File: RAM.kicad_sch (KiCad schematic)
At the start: 45 parts, among them U1 H3, U3 K4B4G1646E-BYMA 4GB, U4 K4B4G1646E-BYMA 4GB

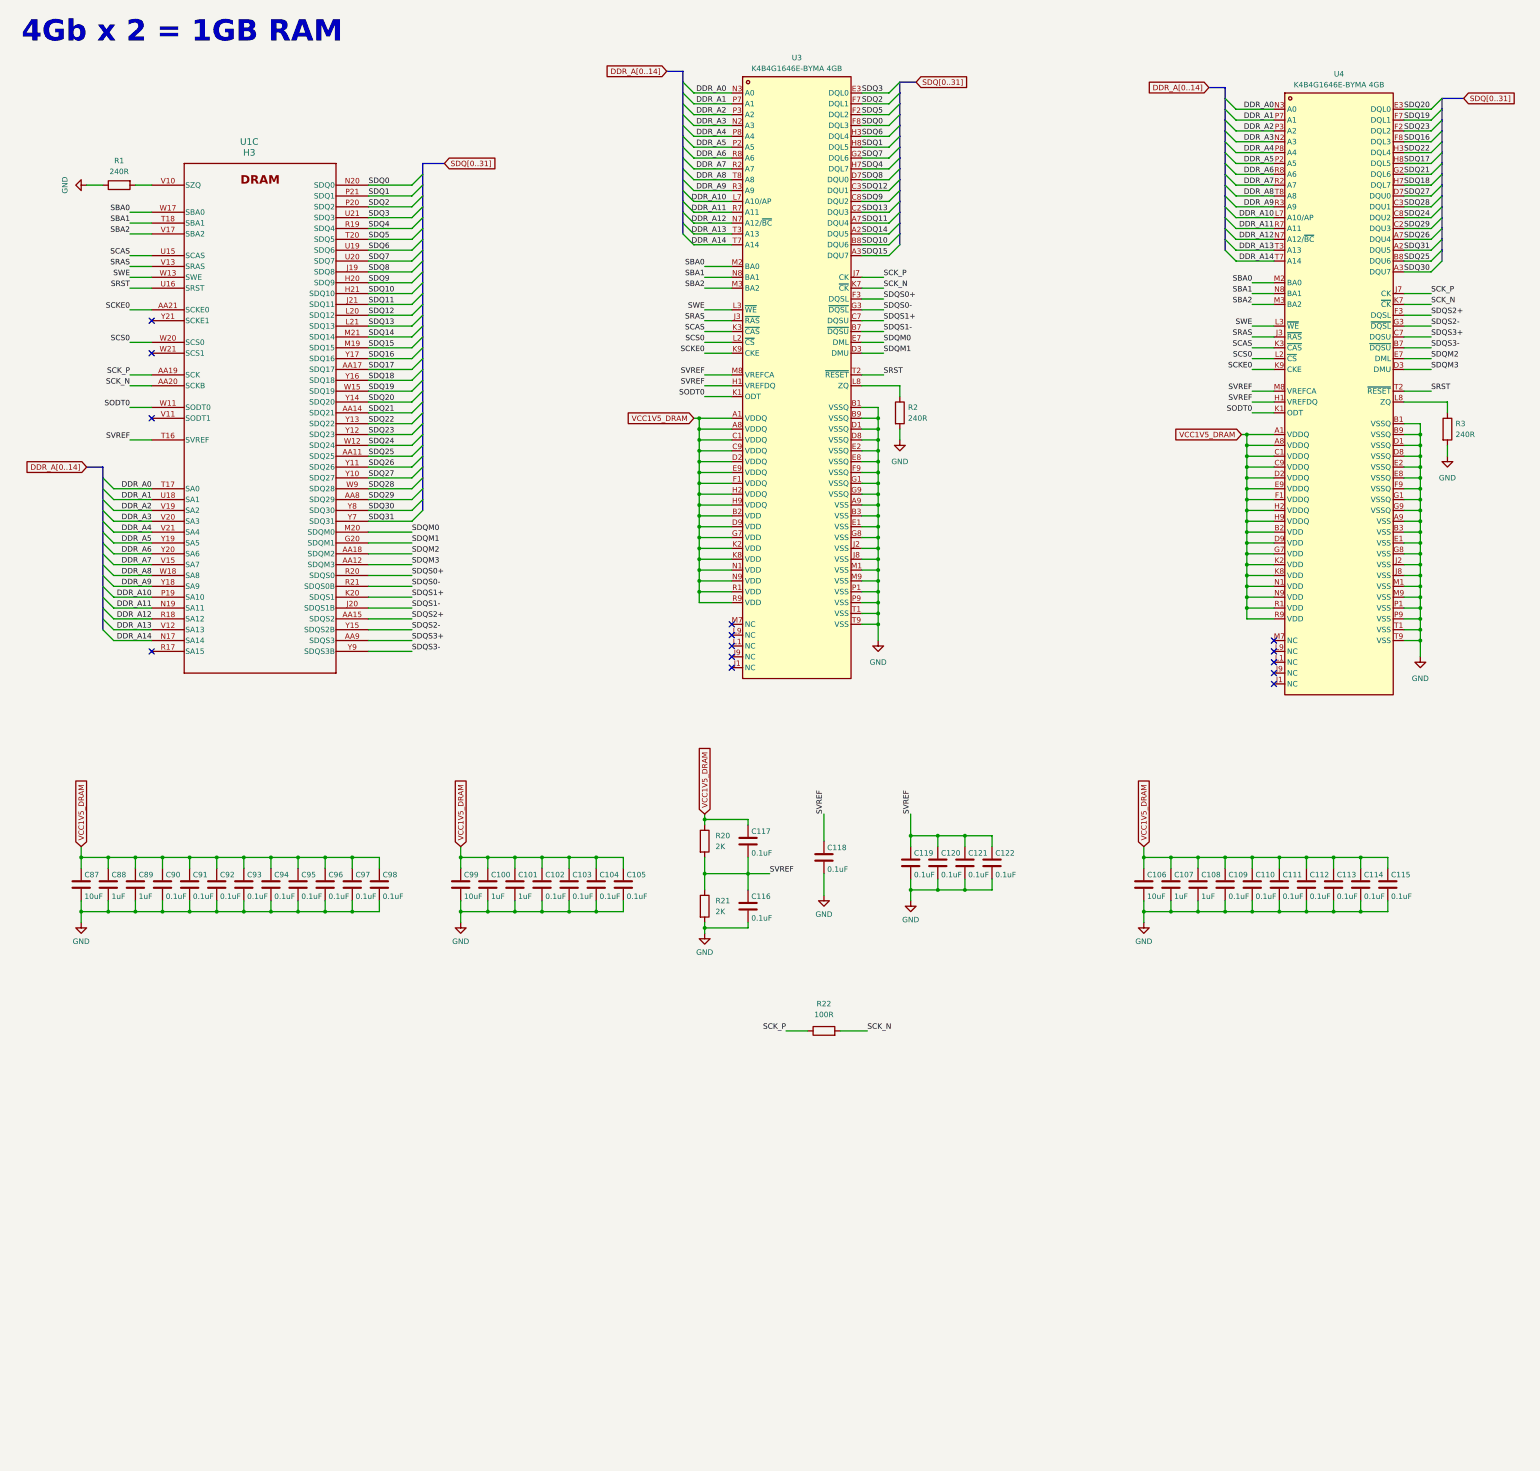
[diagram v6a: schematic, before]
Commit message: switched to one RAM module
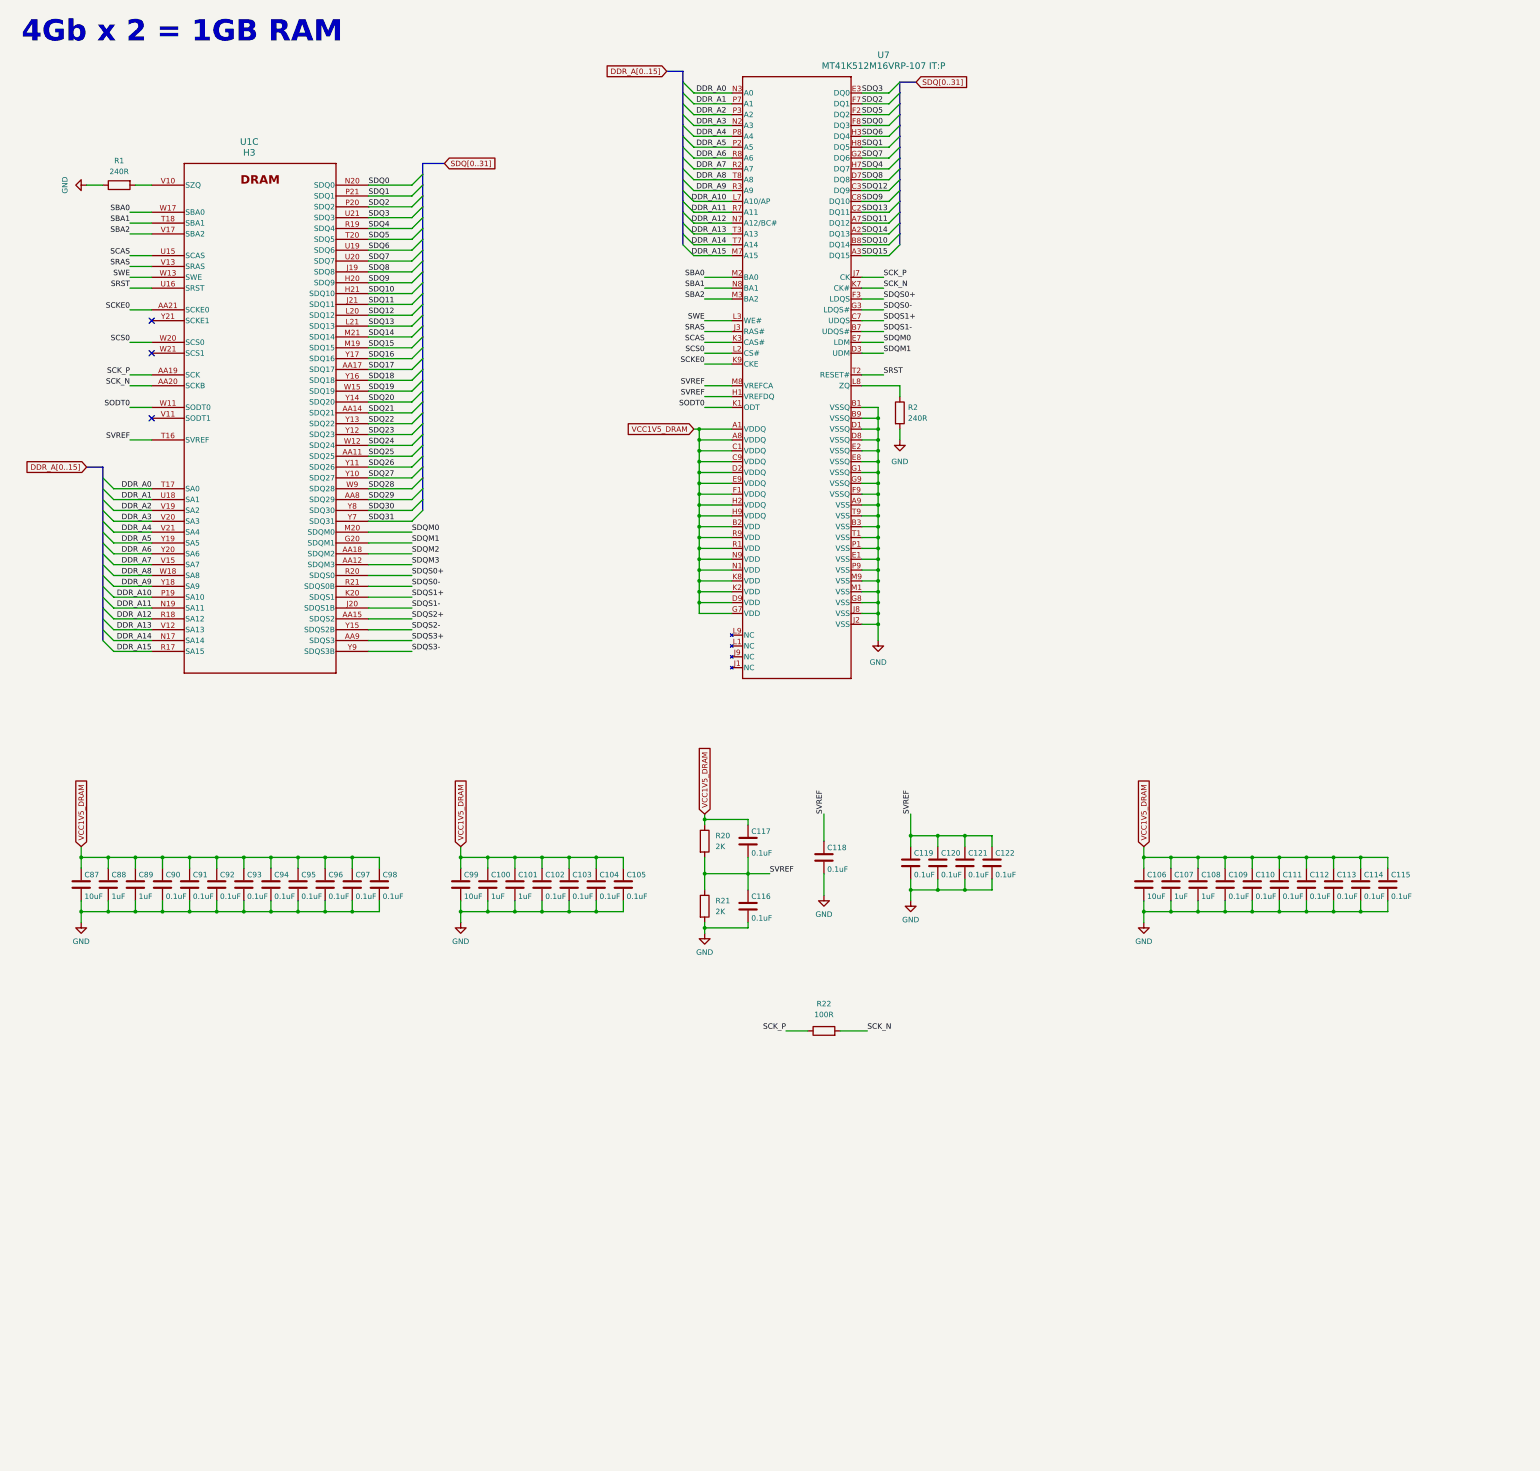
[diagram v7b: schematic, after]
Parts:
- removed R3: 240R, Resistor_SMD:R_0402_1005Metric, symbol Device:R
- removed U3, U4: K4B4G1646E-BYMA 4GB, easyeda2kicad:FBGA-96_L13.5-W7.5-R16-C6-P0.80-TL, symbol easyeda2kicad:K4B4G1646E-BYMA4GB
- added U7: MT41K512M16VRP-107 IT:P, FBGA96_MRN, symbol 2025-04-11_02-15-51:MT41K512M16VRP-107_IT_P
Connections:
- net DDR_A0: now also U7.N3 (A0)
- net DDR_A1: now also U7.P7 (A1)
- net DDR_A10: now also U7.L7 (A10/AP)
- net DDR_A11: now also U7.R7 (A11)
- net DDR_A12: now also U7.N7 (A12/BC#)
- net DDR_A13: now also U7.T3 (A13)
- net DDR_A14: now also U7.T7 (A14)
- net DDR_A2: now also U7.P3 (A2)
- net DDR_A3: now also U7.N2 (A3)
- net DDR_A4: now also U7.P8 (A4)
- net DDR_A5: now also U7.P2 (A5)
- net DDR_A6: now also U7.R8 (A6)
- net DDR_A7: now also U7.R2 (A7)
- net DDR_A8: now also U7.T8 (A8)
- net DDR_A9: now also U7.R3 (A9)
- net GND: now also U7.A9 (VSS), U7.B1 (VSSQ), U7.B3 (VSS), U7.B9 (VSSQ), U7.D1 (VSSQ), U7.D8 (VSSQ), U7.E1 (VSS), U7.E2 (VSSQ), U7.E8 (VSSQ), U7.F9 (VSSQ), U7.G1 (VSSQ), U7.G8 (VSS), U7.G9 (VSSQ), U7.J2 (VSS), U7.J8 (VSS), U7.M1 (VSS), U7.M9 (VSS), U7.P1 (VSS), U7.P9 (VSS), U7.T1 (VSS), U7.T9 (VSS)
- net SBA0: now also U7.M2 (BA0)
- net SBA1: now also U7.N8 (BA1)
- net SBA2: now also U7.M3 (BA2)
- net SCAS: now also U7.K3 (CAS#)
- net SCKE0: now also U7.K9 (CKE)
- net SCK_N: now also U7.K7 (CK#)
- net SCK_P: now also U7.J7 (CK)
- net SCS0: now also U7.L2 (CS#)
- net SDQ0: now also U7.F8 (DQ3)
- net SDQ1: now also U7.H8 (DQ5)
- net SDQ10: now also U7.B8 (DQ14)
- net SDQ11: now also U7.A7 (DQ12)
- net SDQ12: now also U7.C3 (DQ9)
- net SDQ13: now also U7.C2 (DQ11)
- net SDQ14: now also U7.A2 (DQ13)
- net SDQ15: now also U7.A3 (DQ15)
- net SDQ2: now also U7.F7 (DQ1)
- net SDQ3: now also U7.E3 (DQ0)
- net SDQ4: now also U7.H7 (DQ7)
- net SDQ5: now also U7.F2 (DQ2)
- net SDQ6: now also U7.H3 (DQ4)
- net SDQ7: now also U7.G2 (DQ6)
- net SDQ8: now also U7.D7 (DQ8)
- net SDQ9: now also U7.C8 (DQ10)
- net SDQM0: now also U7.E7 (LDM)
- net SDQM1: now also U7.D3 (UDM)
- net SDQS0+: now also U7.F3 (LDQS)
- net SDQS0-: now also U7.G3 (LDQS#)
- net SDQS1+: now also U7.C7 (UDQS)
- net SDQS1-: now also U7.B7 (UDQS#)
- net SODT0: now also U7.K1 (ODT)
- net SRAS: now also U7.J3 (RAS#)
- net SRST: now also U7.T2 (RESET#)
- net SVREF: now also U7.H1 (VREFDQ), U7.M8 (VREFCA)
- net SWE: now also U7.L3 (WE#)
- net VCC1V5_DRAM: now also U7.A1 (VDDQ), U7.A8 (VDDQ), U7.B2 (VDD), U7.C1 (VDDQ), U7.C9 (VDDQ), U7.D2 (VDDQ), U7.D9 (VDD), U7.E9 (VDDQ), U7.F1 (VDDQ), U7.G7 (VDD), U7.H2 (VDDQ), U7.H9 (VDDQ), U7.K2 (VDD), U7.K8 (VDD), U7.N1 (VDD), U7.N9 (VDD), U7.R1 (VDD), U7.R9 (VDD)
- net at R2.1: now also U7.L8 (ZQ)
- net DDR_A15: now reaches U1.R17 (SA15)
- net DDR_A15: now also U7.M7 (A15)
- no-connect marks 14 -> 3

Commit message: RAM routing additions
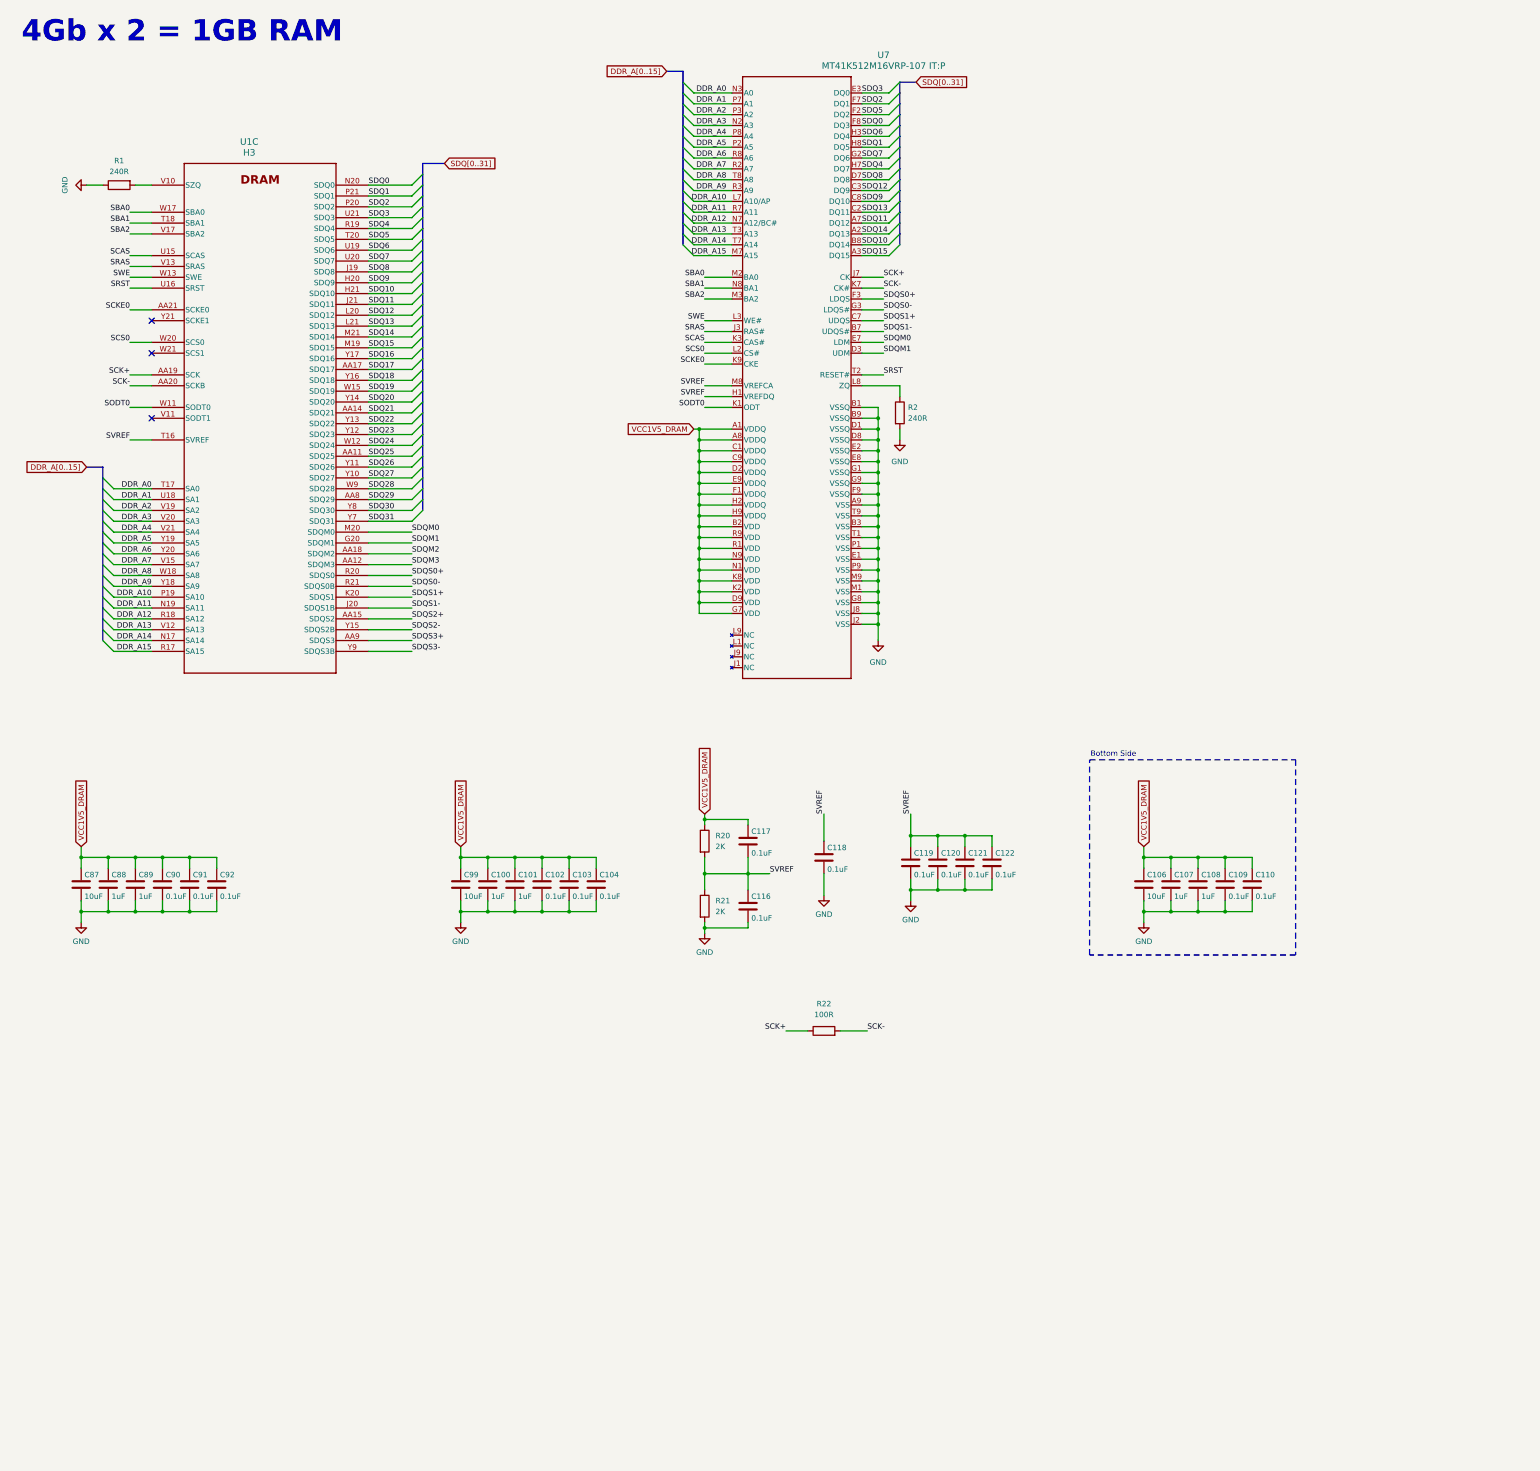
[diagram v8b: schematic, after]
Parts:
- removed C105, C111, C112, C113, C114, C115, C93, C94, C95, C96, C97, C98: 0.1uF, Capacitor_SMD:C_0402_1005Metric, symbol Device:C
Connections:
- net SCK_N renamed SCK-
- net SCK_P renamed SCK+
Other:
- note added: "Bottom Side"
